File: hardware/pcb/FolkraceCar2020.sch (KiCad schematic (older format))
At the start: 74 parts, among them IC1 DRV8874PWPR, J1 Conn_01x02_Male, J2 Raspberry_Pi, J3 Conn_01x02_Male, J4 Conn Servo, J5 Conn Fan, J6 Conn Hall Effect, J7 Conn_01x06_Male, J8 Conn_01x06_Male, J9 Conn_01x06_Male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

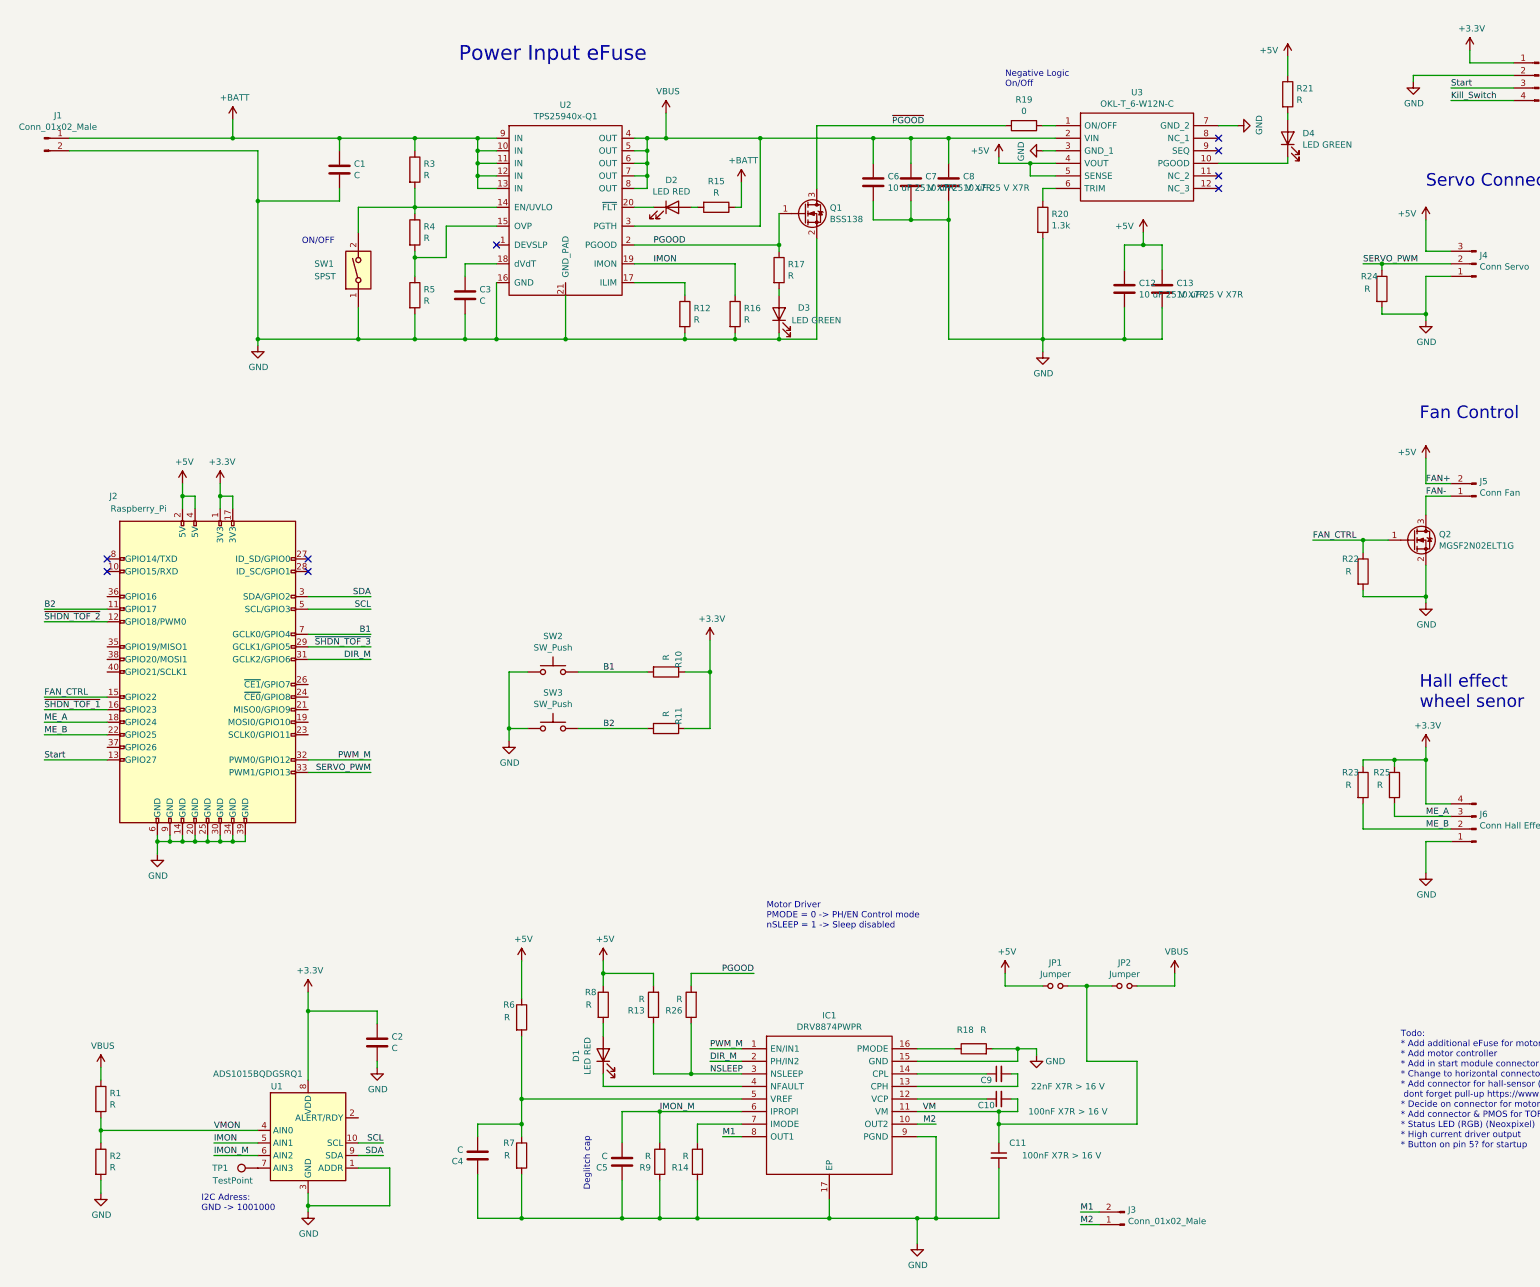
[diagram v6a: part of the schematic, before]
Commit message: added notes and values to components
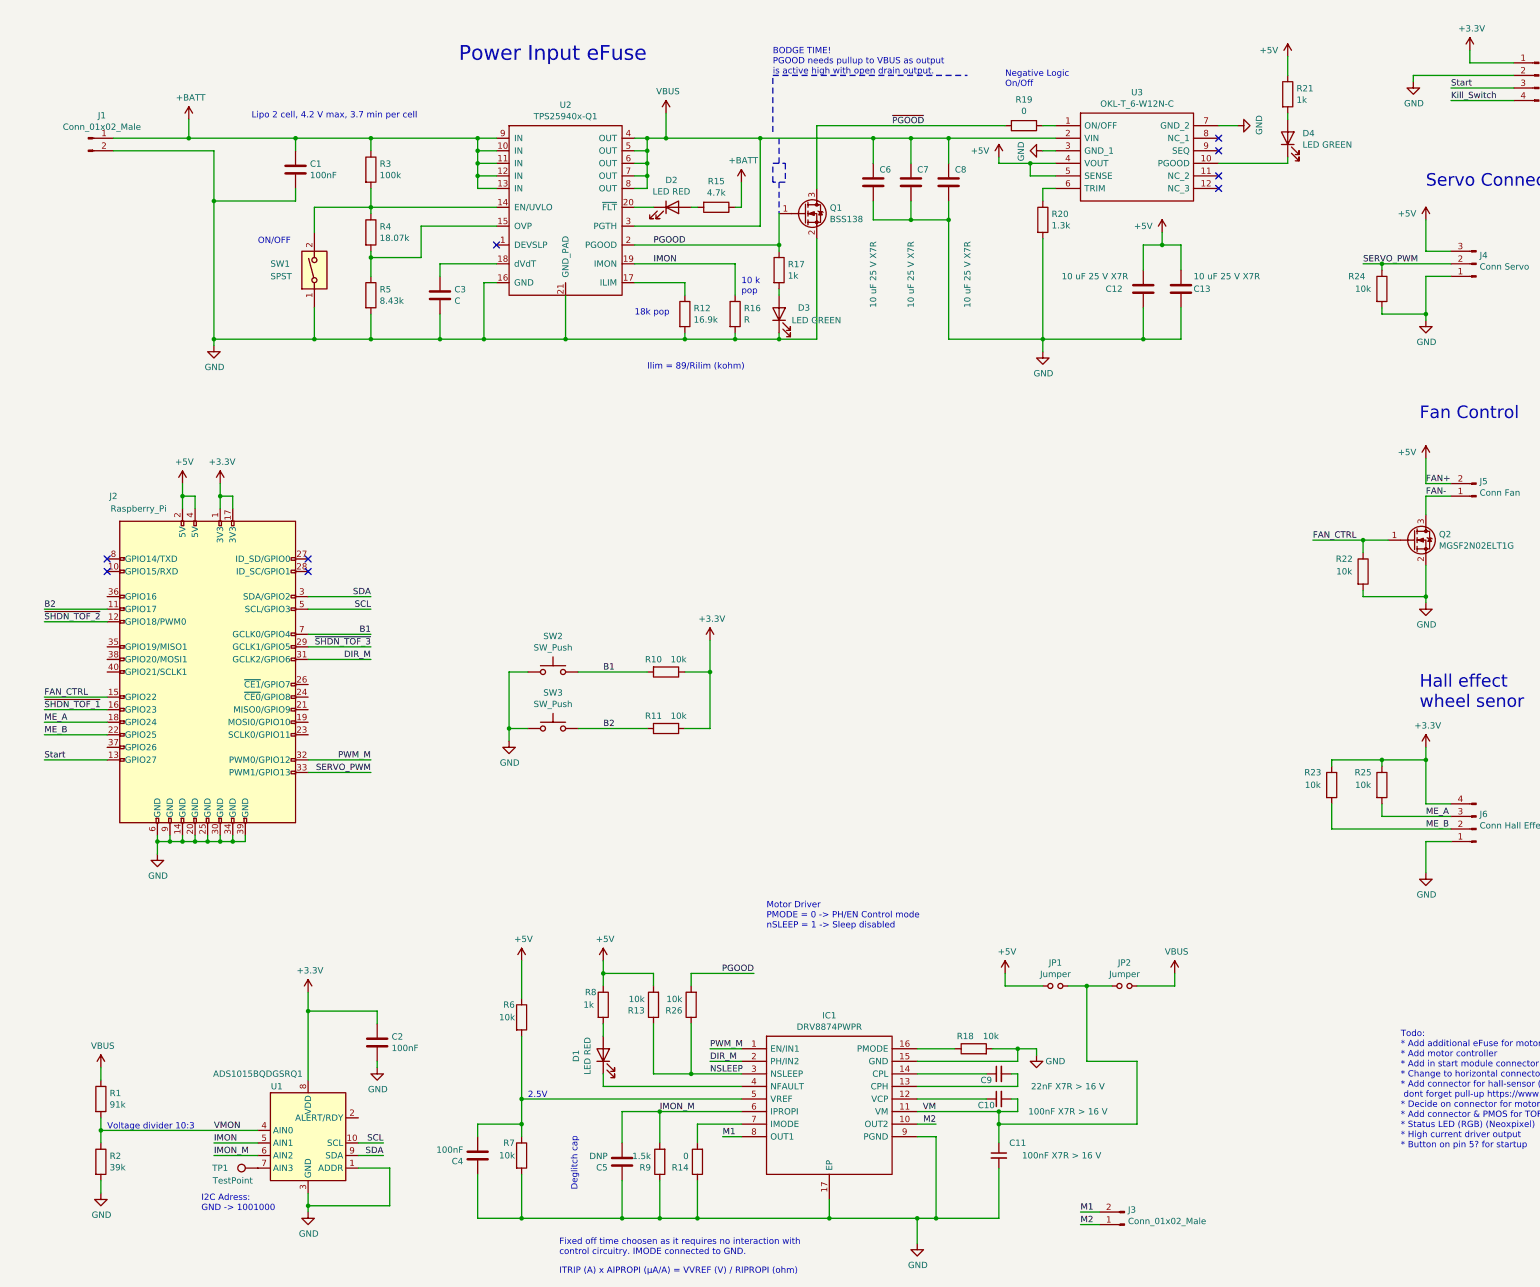
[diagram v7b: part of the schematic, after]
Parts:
- C1, C2, C4: value C -> 100nF
- C5: value C -> DNP
- R1: value R -> 91k
- R10, R11, R13, R18, R22, R23, R24, R25, R26, R6, R7: value R -> 10k
- R12: value R -> 16.9k
- R14: value R -> 0
- R15: value R -> 4.7k
- R17, R21, R8: value R -> 1k
- R2: value R -> 39k
- R3: value R -> 100k
- R4: value R -> 18.07k
- R5: value R -> 8.43k
- R9: value R -> 1.5k
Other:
- note added: "10 k\npop"
- note added: "18k pop\n\n"
- note added: "2.5V"
- note added: "BODGE TIME!\nPGOOD needs pullup to VBUS as output\nis active high with open drain output."
- note added: "Fixed off time choosen as it requires no interaction with\ncontrol circuitry. IMODE connected to GND."
- note added: "ITRIP (A) x AIPROPI (μA/A) = VVREF (V) / RIPROPI (ohm)"
- note added: "Ilim = 89/Rilim (kohm)"
- note added: "Lipo 2 cell, 4.2 V max, 3.7 min per cell"
- note added: "Voltage divider 10:3"
- moved on the sheet: C1, C12, C13, C3, J1, R23, R25, R3, R4, R5, SW1
